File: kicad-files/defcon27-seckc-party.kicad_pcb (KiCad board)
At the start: 2 copper layers, 74.6 x 71.2 mm, 3 parts

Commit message: final design
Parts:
- removed the G*** at (0.00, 0.00) (x3)
- added G*** (x5): LOGO, LOGO, F.Cu at (0.00, 0.00)

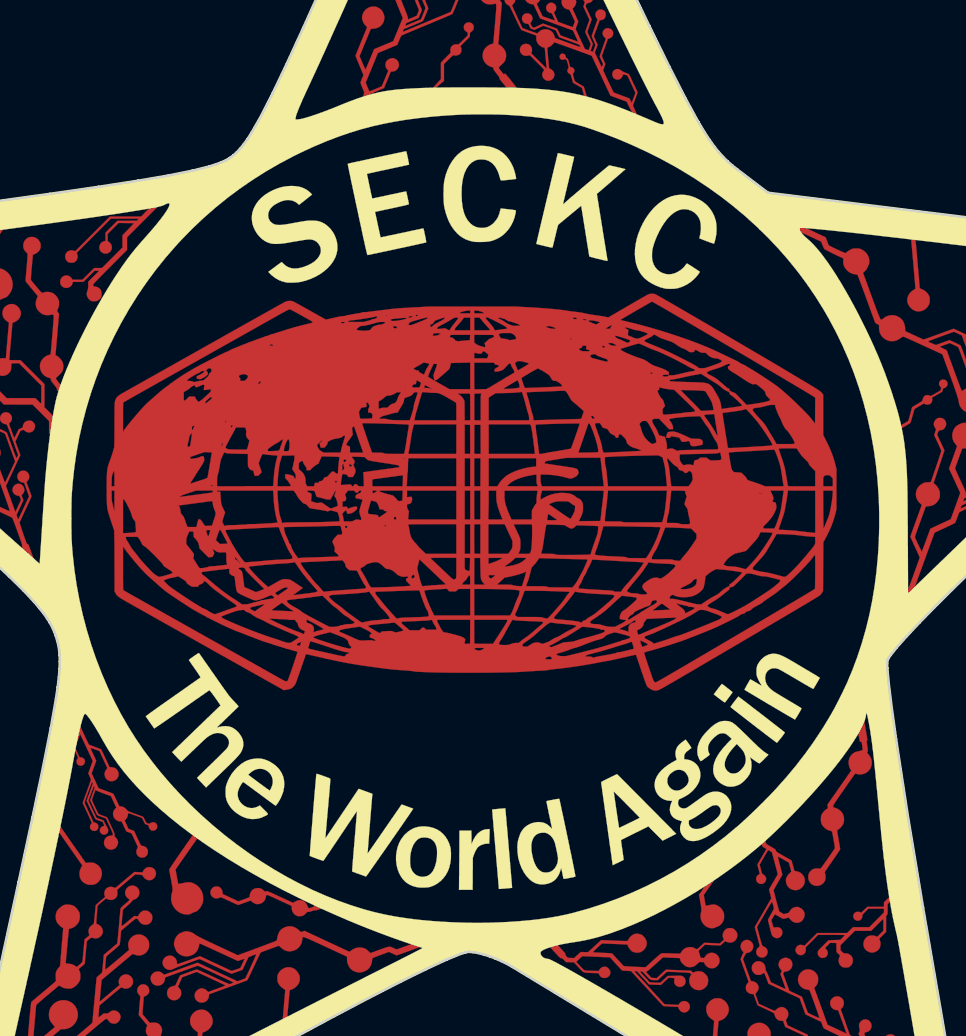
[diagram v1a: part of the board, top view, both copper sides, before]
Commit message: updated font to Rye and made fonts smaller for both texts
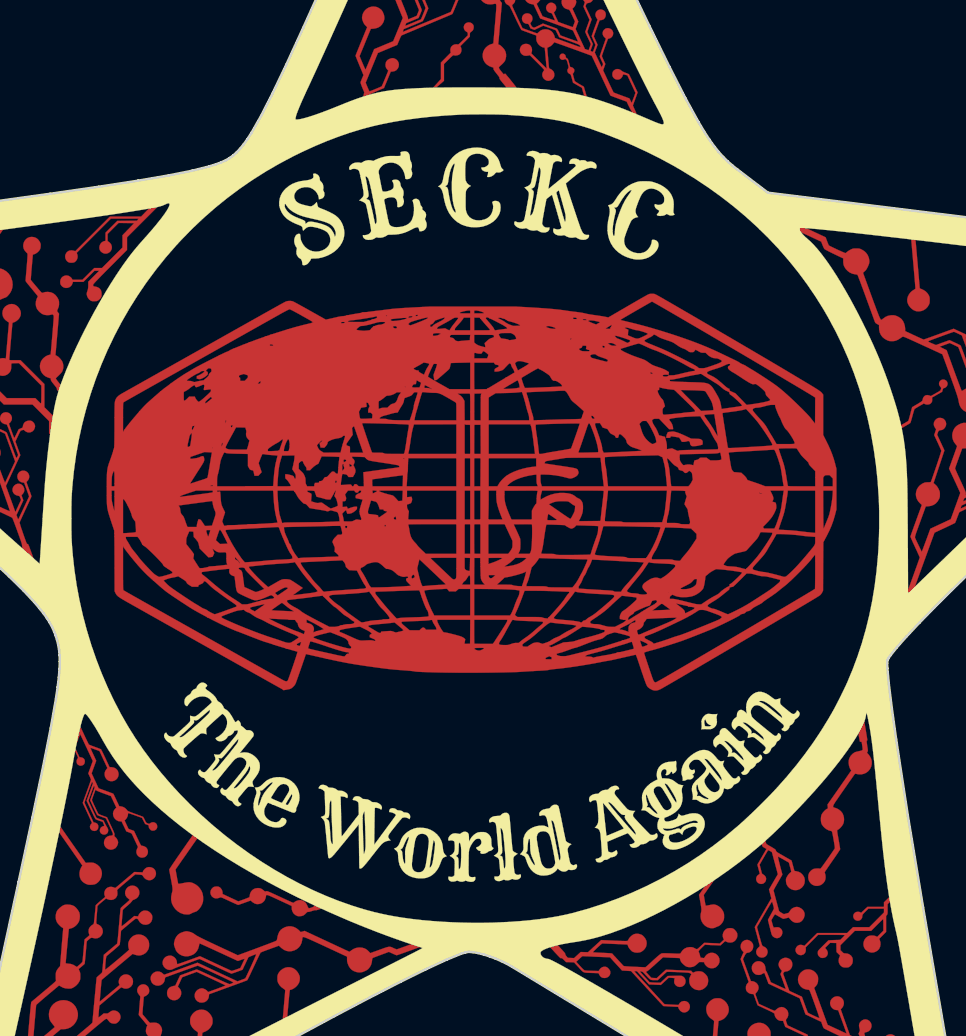
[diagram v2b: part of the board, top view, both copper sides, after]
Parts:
- removed the G*** at (0.00, 0.00) (x5)
- added G*** (x5): LOGO, LOGO, F.Cu at (0.00, 0.00)
